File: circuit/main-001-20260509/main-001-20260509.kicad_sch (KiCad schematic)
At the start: 20 parts, among them J1 Conn_Relay, J2 Conn_Sub, Q1 BSS138, Q2 BSS138, SW1 RESET, U1 DEV-16771, U2 BNO055

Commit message: Update メイン基板の修正を完了させた
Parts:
- D1: value LED_Small -> D13
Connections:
- net +3.3V: now also J1.9 (Pin_9); no longer J1.10 (Pin_10)
- net Motor4_{PWM}: now also J1.10 (Pin_10); no longer J1.9 (Pin_9)
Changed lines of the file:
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@@
 	(wire
 		(pts
-			(xy 144.78 71.12) (xy 137.16 71.12)
-		)
-		(stroke
-			(width 0)
-			(type default)
-		)
-	)
-	(wire
-		(pts
 			(xy 46.99 165.1) (xy 46.99 167.64)
 		)
@@
 	(wire
 		(pts
-			(xy 142.24 63.5) (xy 142.24 78.74)
+			(xy 139.7 63.5) (xy 139.7 78.74)
 		)
 		(stroke
@@
 	(wire
 		(pts
+			(xy 121.92 76.2) (xy 124.46 76.2)
+		)
+		(stroke
+			(width 0)
+			(type default)
+		)
+	)
+	(wire
+		(pts
 			(xy 68.58 39.37) (xy 71.12 39.37)
 		)
@@
 	(wire
 		(pts
-			(xy 144.78 86.36) (xy 137.16 86.36)
+			(xy 142.24 86.36) (xy 137.16 86.36)
 		)
 		(stroke
@@
 	(wire
 		(pts
-			(xy 137.16 81.28) (xy 144.78 81.28)
+			(xy 137.16 81.28) (xy 142.24 81.28)
 		)
 		(stroke
@@
 	(wire
 		(pts
+			(xy 137.16 73.66) (xy 142.24 73.66)
+		)
+		(stroke
+			(width 0)
+			(type default)
+		)
+	)
+	(wire
+		(pts
 			(xy 38.1 74.93) (xy 40.64 74.93)
 		)
@@
 	(wire
 		(pts
-			(xy 144.78 83.82) (xy 137.16 83.82)
+			(xy 142.24 83.82) (xy 137.16 83.82)
 		)
 		(stroke
@@
 	(wire
 		(pts
-			(xy 144.78 66.04) (xy 137.16 66.04)
-		)
-		(stroke
-			(width 0)
-			(type default)
-		)
-	)
-	(wire
-		(pts
-			(xy 144.78 73.66) (xy 137.16 73.66)
-		)
-		(stroke
-			(width 0)
-			(type default)
-		)
-	)
-	(wire
-		(pts
 			(xy 194.31 107.95) (xy 194.31 110.49)
 		)
@@
 	(wire
 		(pts
-			(xy 142.24 78.74) (xy 137.16 78.74)
+			(xy 139.7 78.74) (xy 137.16 78.74)
 		)
 		(stroke
@@
 	(wire
 		(pts
-			(xy 144.78 68.58) (xy 137.16 68.58)
-		)
-		(stroke
-			(width 0)
-			(type default)
-		)
-	)
-	(wire
-		(pts
 			(xy 68.58 46.99) (xy 71.12 46.99)
 		)
@@
 	(wire
 		(pts
-			(xy 38.1 64.77) (xy 40.64 64.77)
+			(xy 121.92 64.77) (xy 121.92 76.2)
 		)
 		(stroke
@@
 	(wire
 		(pts
-			(xy 139.7 63.5) (xy 139.7 76.2)
+			(xy 38.1 64.77) (xy 40.64 64.77)
 		)
 		(stroke
@@
 	(wire
 		(pts
+			(xy 137.16 71.12) (xy 142.24 71.12)
+		)
+		(stroke
+			(width 0)
+			(type default)
+		)
+	)
+	(wire
+		(pts
 			(xy 111.76 38.1) (xy 114.3 38.1)
 		)
@@
 	(wire
 		(pts
+			(xy 137.16 66.04) (xy 142.24 66.04)
+		)
+		(stroke
+			(width 0)
+			(type default)
+		)
+	)
+	(wire
+		(pts
 			(xy 68.58 41.91) (xy 71.12 41.91)
 		)
@@
 	(wire
 		(pts
-			(xy 119.38 76.2) (xy 124.46 76.2)
-		)
-		(stroke
-			(width 0)
-			(type default)
-		)
-	)
-	(wire
-		(pts
 			(xy 189.23 72.39) (xy 181.61 72.39)
 		)
@@
 	(wire
 		(pts
-			(xy 139.7 76.2) (xy 137.16 76.2)
+			(xy 137.16 76.2) (xy 142.24 76.2)
 		)
 		(stroke
@@
 	(wire
 		(pts
+			(xy 137.16 68.58) (xy 142.24 68.58)
+		)
+		(stroke
+			(width 0)
+			(type default)
+		)
+	)
+	(wire
+		(pts
 			(xy 68.58 64.77) (xy 71.12 64.77)
 		)
@@
 	(global_label "Motor4_{PWM}"
 		(shape input)
-		(at 119.38 76.2 180)
+		(at 142.24 76.2 0)
 		(fields_autoplaced yes)
 		(effects
@@
 				(size 1.27 1.27)
 			)
-			(justify right)
+			(justify left)
 		)
 		(property "Intersheetrefs" "${INTERSHEET_REFS}"
-			(at 106.535 76.2 0)
+			(at 155.085 76.2 0)
 			(hide yes)
 			(show_name no)
@@
 					(size 1.27 1.27)
 				)
-				(justify right)
+				(justify left)
 			)
 		)
@@
 	(global_label "EN_{BOOST}"
 		(shape input)
-		(at 144.78 86.36 0)
+		(at 142.24 86.36 0)
 		(fields_autoplaced yes)
 		(effects
@@
 		)
 		(property "Intersheetrefs" "${INTERSHEET_REFS}"
-			(at 155.182 86.36 0)
+			(at 152.642 86.36 0)
 			(hide yes)
 			(show_name no)
@@
 	(global_label "BallCatch_{Back}"
 		(shape output)
-		(at 144.78 81.28 0)
+		(at 142.24 81.28 0)
 		(fields_autoplaced yes)
 		(effects
@@
 		)
 		(property "Intersheetrefs" "${INTERSHEET_REFS}"
-			(at 157.6722 81.28 0)
+			(at 155.1322 81.28 0)
 			(hide yes)
 			(show_name no)
@@
 	(global_label "RX_{teensy}-TX_{Arduino}-5V"
 		(shape output)
-		(at 144.78 68.58 0)
+		(at 142.24 68.58 0)
 		(fields_autoplaced yes)
 		(effects
@@
 		)
 		(property "Intersheetrefs" "${INTERSHEET_REFS}"
-			(at 168.3634 68.58 0)
+			(at 165.8234 68.58 0)
 			(hide yes)
 			(show_name no)
@@
 	(global_label "PH_{Dribbler-Front}"
 		(shape input)
-		(at 144.78 71.12 0)
+		(at 142.24 71.12 0)
 		(fields_autoplaced yes)
 		(effects
@@
 		)
 		(property "Intersheetrefs" "${INTERSHEET_REFS}"
-			(at 157.0233 71.12 0)
+			(at 154.4833 71.12 0)
 			(hide yes)
 			(show_name no)
@@
 	(global_label "TX_{teensy}-RX_{Arduino}-5V"
 		(shape input)
-		(at 144.78 66.04 0)
+		(at 142.24 66.04 0)
 		(fields_autoplaced yes)
 		(effects
@@
 		)
 		(property "Intersheetrefs" "${INTERSHEET_REFS}"
-			(at 168.3634 66.04 0)
+			(at 165.8234 66.04 0)
 			(hide yes)
 			(show_name no)
@@
 	(global_label "EN_{Dribbler-Front}"
 		(shape input)
-		(at 144.78 73.66 0)
+		(at 142.24 73.66 0)
 		(fields_autoplaced yes)
 		(effects
@@
 		)
 		(property "Intersheetrefs" "${INTERSHEET_REFS}"
-			(at 157.0233 73.66 0)
+			(at 154.4833 73.66 0)
 			(hide yes)
 			(show_name no)
@@
 	(global_label "Kick_{Chip}"
 		(shape input)
-		(at 144.78 83.82 0)
+		(at 142.24 83.82 0)
 		(fields_autoplaced yes)
 		(effects
@@
 		)
 		(property "Intersheetrefs" "${INTERSHEET_REFS}"
-			(at 153.2378 83.82 0)
+			(at 150.6978 83.82 0)
 			(hide yes)
 			(show_name no)
@@
 	(symbol
 		(lib_id "power:+5V")
-		(at 142.24 63.5 0)
+		(at 139.7 63.5 0)
 		(unit 1)
 		(body_style 1)
@@
 		(dnp no)
 		(property "Reference" "#PWR020"
-			(at 142.24 67.31 0)
+			(at 139.7 67.31 0)
 			(hide yes)
 			(show_name no)
@@
 		)
 		(property "Value" "+5V"
-			(at 146.05 62.23 0)
+			(at 143.51 62.23 0)
 			(show_name no)
 			(do_not_autoplace no)
@@
 		)
 		(property "Footprint" ""
-			(at 142.24 63.5 0)
+			(at 139.7 63.5 0)
 			(hide yes)
 			(show_name no)
@@
 		)
 		(property "Datasheet" ""
-			(at 142.24 63.5 0)
+			(at 139.7 63.5 0)
 			(hide yes)
 			(show_name no)
@@
 		)
 		(property "Description" "Power symbol creates a global label with name \"+5V\""
-			(at 142.24 63.5 0)
+			(at 139.7 63.5 0)
 			(hide yes)
 			(show_name no)
@@
 	(symbol
 		(lib_id "power:+3.3V")
-		(at 139.7 63.5 0)
+		(at 121.92 64.77 0)
 		(unit 1)
 		(body_style 1)
@@
 		(fields_autoplaced yes)
 		(property "Reference" "#PWR010"
-			(at 139.7 67.31 0)
+			(at 121.92 68.58 0)
 			(hide yes)
 			(show_name no)
@@
 		)
 		(property "Value" "+3.3V"
-			(at 139.7 58.42 0)
+			(at 121.92 59.69 0)
 			(show_name no)
 			(do_not_autoplace no)
@@
 		)
 		(property "Footprint" ""
-			(at 139.7 63.5 0)
+			(at 121.92 64.77 0)
 			(hide yes)
 			(show_name no)
@@
 		)
 		(property "Datasheet" ""
-			(at 139.7 63.5 0)
+			(at 121.92 64.77 0)
 			(hide yes)
 			(show_name no)
@@
 		)
 		(property "Description" "Power symbol creates a global label with name \"+3.3V\""
-			(at 139.7 63.5 0)
+			(at 121.92 64.77 0)
 			(hide yes)
 			(show_name no)
@@
 			)
 		)
-		(property "Value" "LED_Small"
+		(property "Value" "D13"
 			(at 196.85 121.8564 90)
 			(show_name no)

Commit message: Update メイン基板に使用するFPCコネクタを変更・修正
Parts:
- J2: footprint @Thrive_footprint_main:FPC-05F-18PH20 -> @Thrive_footprint_main:AFC01-S18FCA-00
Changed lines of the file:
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@@
 			)
 		)
-		(property "Footprint" "@Thrive_footprint_main:FPC-05F-18PH20"
+		(property "Footprint" "@Thrive_footprint_main:AFC01-S18FCA-00"
 			(at 176.53 54.61 0)
 			(hide yes)

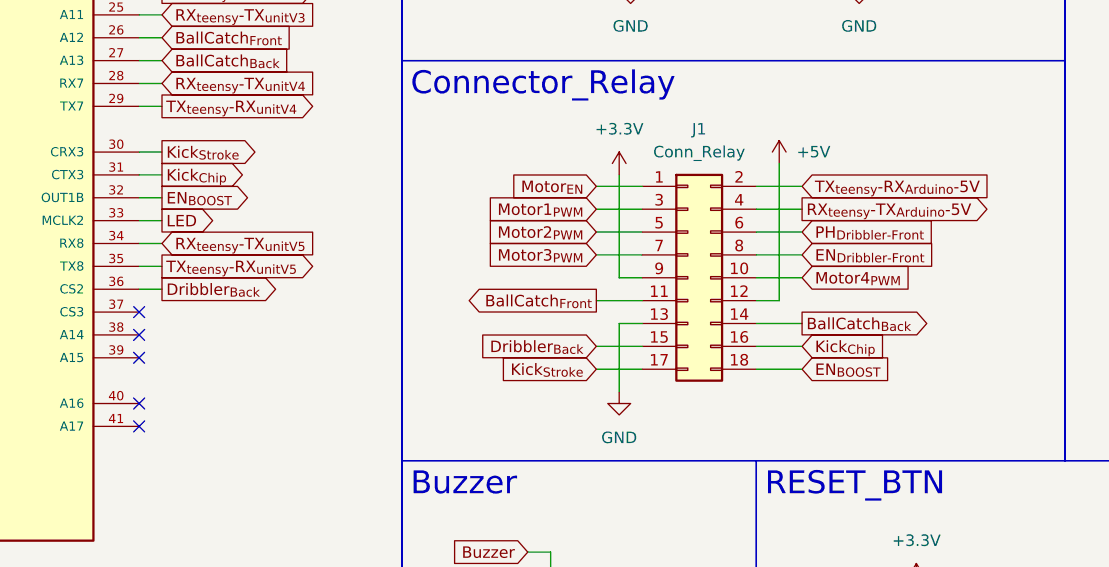
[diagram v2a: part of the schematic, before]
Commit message: Update メイン基板のシルクスクリーンを修正した
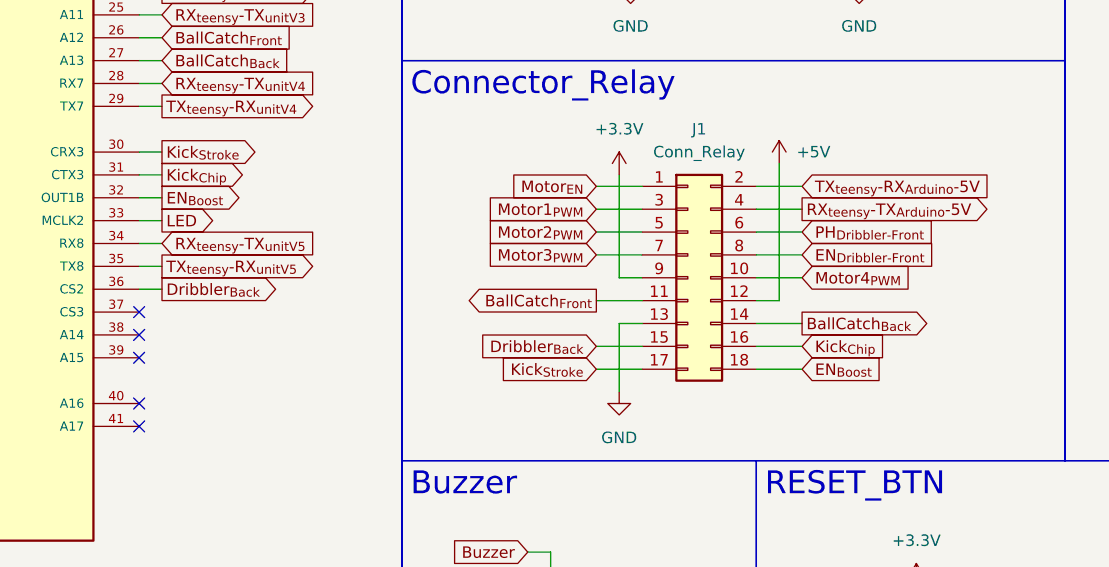
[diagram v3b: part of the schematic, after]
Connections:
- net EN_{BOOST} renamed EN_{Boost}
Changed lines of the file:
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@@
 		)
 	)
-	(global_label "EN_{BOOST}"
+	(global_label "EN_{Boost}"
 		(shape output)
 		(at 71.12 67.31 0)
@@
 		)
 		(property "Intersheetrefs" "${INTERSHEET_REFS}"
-			(at 81.0667 67.31 0)
+			(at 80.2465 67.31 0)
 			(hide yes)
 			(show_name no)
@@
 		)
 	)
-	(global_label "EN_{BOOST}"
+	(global_label "EN_{Boost}"
 		(shape input)
 		(at 142.24 86.36 0)
@@
 		)
 		(property "Intersheetrefs" "${INTERSHEET_REFS}"
-			(at 152.642 86.36 0)
+			(at 151.3665 86.36 0)
 			(hide yes)
 			(show_name no)

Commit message: Update メイン基板の発注ファイルを更新
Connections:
- net +5V: no longer J2.11 (Pin_11)
- net GND: now also J2.11 (Pin_11)
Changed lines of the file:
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@@
 	)
 	(junction
+		(at 184.15 62.23)
+		(diameter 0)
+		(color 0 0 0 0)
+	)
+	(junction
 		(at 62.23 137.16)
 		(diameter 0)
@@
 	(wire
 		(pts
+			(xy 184.15 59.69) (xy 184.15 62.23)
+		)
+		(stroke
+			(width 0)
+			(type default)
+		)
+	)
+	(wire
+		(pts
 			(xy 40.64 26.67) (xy 38.1 26.67)
 		)
@@
 	(wire
 		(pts
-			(xy 125.73 33.02) (xy 123.19 33.02)
+			(xy 181.61 59.69) (xy 184.15 59.69)
 		)
 		(stroke
@@
 	(wire
 		(pts
-			(xy 186.69 59.69) (xy 186.69 31.75)
+			(xy 125.73 33.02) (xy 123.19 33.02)
 		)
 		(stroke
@@
 	(wire
 		(pts
-			(xy 181.61 59.69) (xy 186.69 59.69)
-		)
-		(stroke
-			(width 0)
-			(type default)
-		)
-	)
-	(wire
-		(pts
 			(xy 137.16 66.04) (xy 142.24 66.04)
 		)
@@
 					(unit 1)
 				)
-			)
-		)
-	)
-	(symbol
-		(lib_id "power:+5V")
-		(at 186.69 31.75 0)
-		(unit 1)
-		(body_style 1)
-		(exclude_from_sim no)
-		(in_bom yes)
-		(on_board yes)
-		(in_pos_files yes)
-		(dnp no)
-		(property "Reference" "#PWR019"
-			(at 186.69 35.56 0)
-			(hide yes)
-			(show_name no)
-			(do_not_autoplace no)
-			(effects
-				(font
-					(size 1.27 1.27)
-				)
-			)
-		)
-		(property "Value" "+5V"
-			(at 190.5 30.48 0)
-			(show_name no)
-			(do_not_autoplace no)
-			(effects
-				(font
-					(size 1.27 1.27)
-				)
-			)
-		)
-		(property "Footprint" ""
-			(at 186.69 31.75 0)
-			(hide yes)
-			(show_name no)
-			(do_not_autoplace no)
-			(effects
-				(font
-					(size 1.27 1.27)
-				)
-			)
-		)
-		(property "Datasheet" ""
-			(at 186.69 31.75 0)
-			(hide yes)
-			(show_name no)
-			(do_not_autoplace no)
-			(effects
-				(font
-					(size 1.27 1.27)
-				)
-			)
-		)
-		(property "Description" "Power symbol creates a global label with name \"+5V\""
-			(at 186.69 31.75 0)
-			(hide yes)
-			(show_name no)
-			(do_not_autoplace no)
-			(effects
-				(font
-					(size 1.27 1.27)
-				)
-			)
-		)
-		(pin "1"
-		)
-		(instances
-			(project "main-001-20260509"
-				(path "/5c093479-ee40-491f-8d87-7ce1a25afb3d"
-					(reference "#PWR019")
-					(unit 1)
-				)

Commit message: Update メイン基板の回路図/ボード図/発注ファイルを更新
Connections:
- net +3.3V: no longer J2.10 (Pin_10)
- net GND: now also J2.10 (Pin_10)
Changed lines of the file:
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@@
 	)
 	(junction
+		(at 184.15 59.69)
+		(diameter 0)
+		(color 0 0 0 0)
+	)
+	(junction
 		(at 46.99 167.64)
 		(diameter 0)
@@
 	(wire
 		(pts
-			(xy 184.15 31.75) (xy 184.15 57.15)
-		)
-		(stroke
-			(width 0)
-			(type default)
-		)
-	)
-	(wire
-		(pts
 			(xy 62.23 167.64) (xy 64.77 167.64)
 		)
@@
 	(wire
 		(pts
+			(xy 184.15 57.15) (xy 184.15 59.69)
+		)
+		(stroke
+			(width 0)
+			(type default)
+		)
+	)
+	(wire
+		(pts
 			(xy 116.84 35.56) (xy 116.84 40.64)
 		)
@@
 					(unit 1)
 				)
-			)
-		)
-	)
-	(symbol
-		(lib_id "power:+3.3V")
-		(at 184.15 31.75 0)
-		(unit 1)
-		(body_style 1)
-		(exclude_from_sim no)
-		(in_bom yes)
-		(on_board yes)
-		(in_pos_files yes)
-		(dnp no)
-		(fields_autoplaced yes)
-		(property "Reference" "#PWR016"
-			(at 184.15 35.56 0)
-			(hide yes)
-			(show_name no)
-			(do_not_autoplace no)
-			(effects
-				(font
-					(size 1.27 1.27)
-				)
-			)
-		)
-		(property "Value" "+3.3V"
-			(at 184.15 26.67 0)
-			(show_name no)
-			(do_not_autoplace no)
-			(effects
-				(font
-					(size 1.27 1.27)
-				)
-			)
-		)
-		(property "Footprint" ""
-			(at 184.15 31.75 0)
-			(hide yes)
-			(show_name no)
-			(do_not_autoplace no)
-			(effects
-				(font
-					(size 1.27 1.27)
-				)
-			)
-		)
-		(property "Datasheet" ""
-			(at 184.15 31.75 0)
-			(hide yes)
-			(show_name no)
-			(do_not_autoplace no)
-			(effects
-				(font
-					(size 1.27 1.27)
-				)
-			)
-		)
-		(property "Description" "Power symbol creates a global label with name \"+3.3V\""
-			(at 184.15 31.75 0)
-			(hide yes)
-			(show_name no)
-			(do_not_autoplace no)
-			(effects
-				(font
-					(size 1.27 1.27)
-				)
-			)
-		)
-		(pin "1"
-		)
-		(instances
-			(project "main-001-20260509"
-				(path "/5c093479-ee40-491f-8d87-7ce1a25afb3d"
-					(reference "#PWR016")
-					(unit 1)
-				)
